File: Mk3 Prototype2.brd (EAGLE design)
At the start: 119.6 x 68 mm, 154 parts, among them IC1 TPD3E001DRL, IC2 TPS62082, IC3 STM32F401V, IC4 BQ24092, IC6 CC3100MOD, IC7 BQ2970, IC8 LSM6DS3, IC9 LIS3MDL, J1 ZX62-AB-5PA(11), J2 ER-TFT024-3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

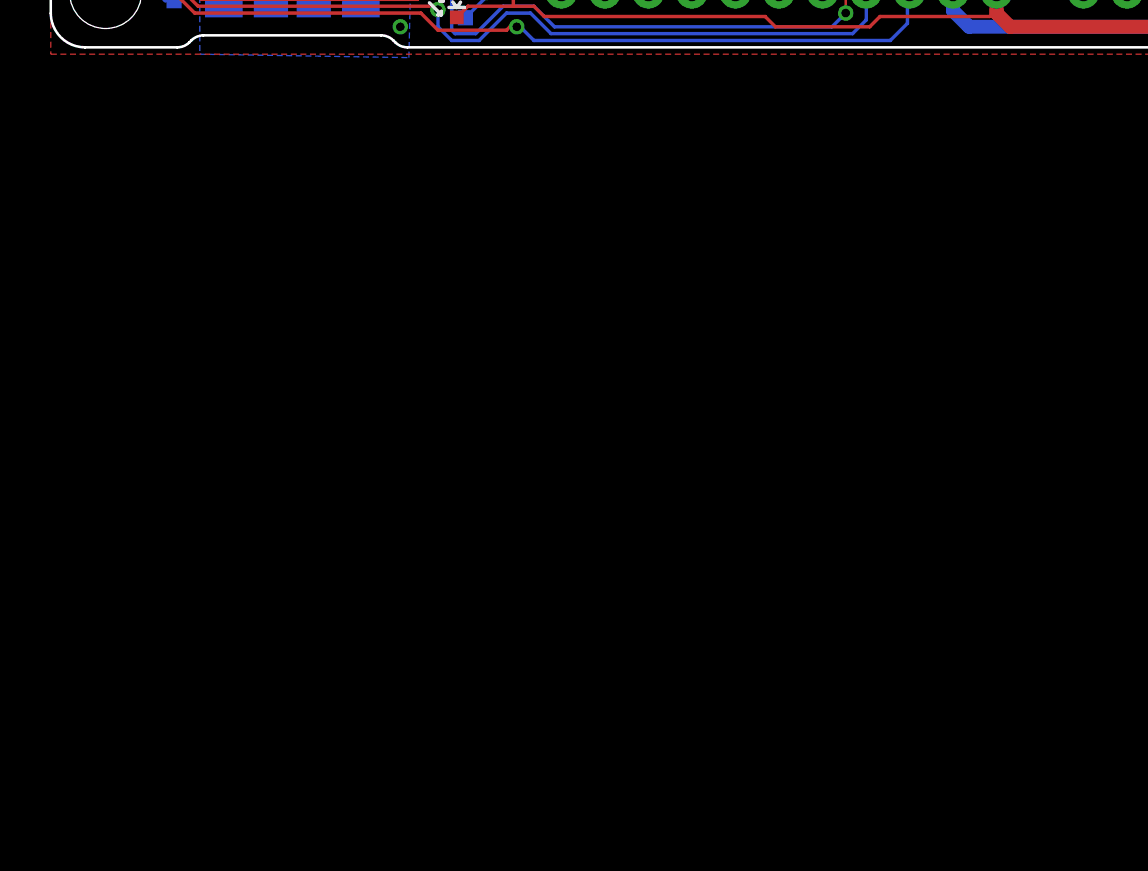
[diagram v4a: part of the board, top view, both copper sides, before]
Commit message: Add full part for LCD out line. update LCD connector to connector part update some resistor parts name
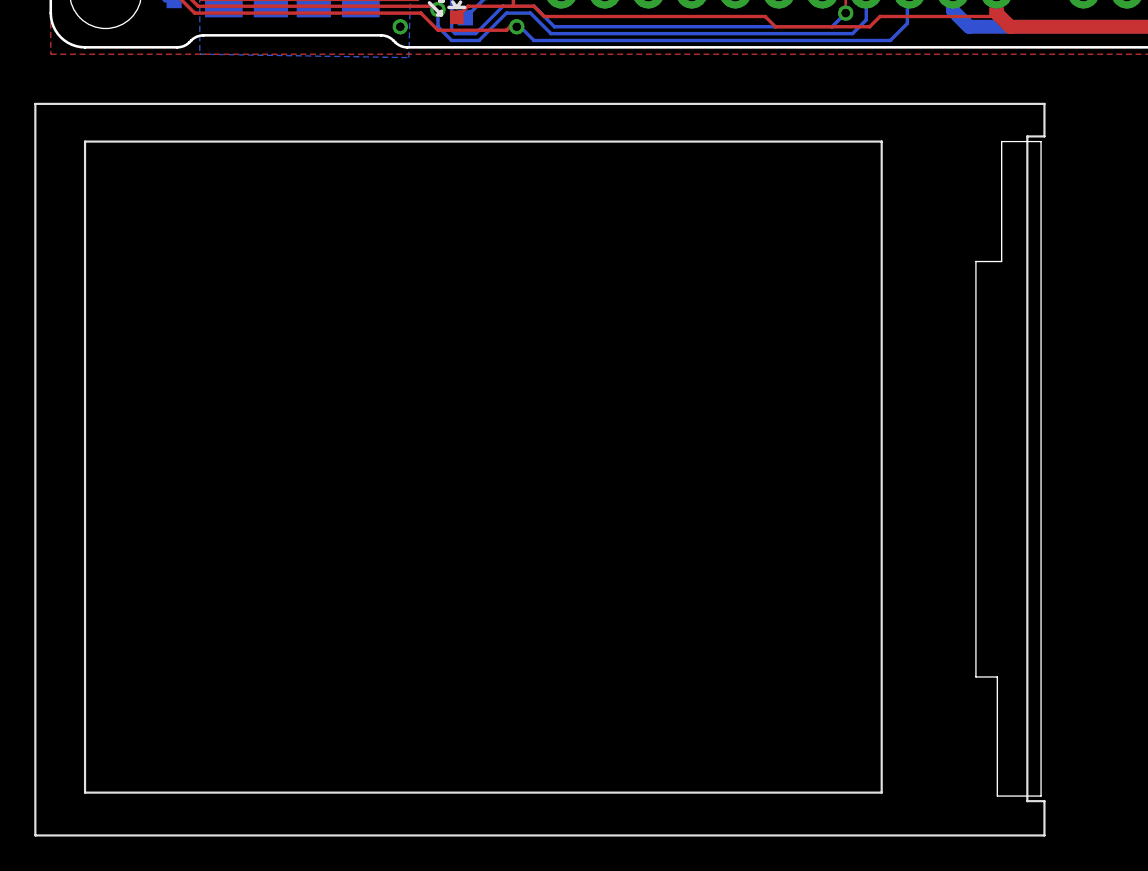
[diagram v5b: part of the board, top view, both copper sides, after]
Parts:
- added U2: ER-TFT024-3, TiLDA Mk3 Parts:ER-TFT024-3
- J2: value ER-TFT024-3 -> ER-CON50HT-1
- R28, R29: value 0603/4.7M/5% -> 0603/4M7/5%
- R44, R47, R48, R49: value 0603/4.7/5% -> 0603/4R7/5%
- U$2: value (none) -> ER-TFT024-3
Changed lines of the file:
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@@
 <variant name="L4" populate="no"/>
 </element>
-<element name="R47" library="TiLDA Mk3 Parts" package="C0603K-SMALL" value="0603/4.7/5%" x="69.6" y="59.2" smashed="yes" rot="MR270">
+<element name="R47" library="TiLDA Mk3 Parts" package="C0603K-SMALL" value="0603/4R7/5%" x="69.6" y="59.2" smashed="yes" rot="MR270">
 <attribute name="NAME" x="69.05" y="54.8" size="1.016" layer="26" font="vector" ratio="14" rot="MR90"/>
 <attribute name="FARNELL" value="9331280" x="69.6" y="59.2" size="1.778" layer="28" rot="MR270" display="off"/>
 <attribute name="FARNELL_REEL" value="2130678" x="69.6" y="59.2" size="1.778" layer="28" rot="MR270" display="off"/>
 </element>
-<element name="R48" library="TiLDA Mk3 Parts" package="C0603K-SMALL" value="0603/4.7/5%" x="71.2" y="59.2" smashed="yes" rot="MR270">
+<element name="R48" library="TiLDA Mk3 Parts" package="C0603K-SMALL" value="0603/4R7/5%" x="71.2" y="59.2" smashed="yes" rot="MR270">
 <attribute name="NAME" x="70.65" y="54.8" size="1.016" layer="26" font="vector" ratio="14" rot="MR90"/>
 <attribute name="FARNELL" value="9331280" x="71.2" y="59.2" size="1.778" layer="28" rot="MR270" display="off"/>
 <attribute name="FARNELL_REEL" value="2130678" x="71.2" y="59.2" size="1.778" layer="28" rot="MR270" display="off"/>
 </element>
-<element name="R49" library="TiLDA Mk3 Parts" package="C0603K-SMALL" value="0603/4.7/5%" x="72.8" y="59.2" smashed="yes" rot="MR270">
+<element name="R49" library="TiLDA Mk3 Parts" package="C0603K-SMALL" value="0603/4R7/5%" x="72.8" y="59.2" smashed="yes" rot="MR270">
 <attribute name="NAME" x="72.25" y="54.8" size="1.016" layer="26" font="vector" ratio="14" rot="MR90"/>
 <attribute name="FARNELL" value="9331280" x="72.8" y="59.2" size="1.778" layer="28" rot="MR270" display="off"/>
@@
 <attribute name="NAME" x="58" y="31.8" size="1.016" layer="26" font="vector" ratio="14" rot="MR0"/>
 </element>
-<element name="J2" library="TiLDA Mk3 Parts" package="FH12-50S-0.5SH" value="ER-TFT024-3" x="65.6" y="41.2" smashed="yes" rot="MR270">
+<element name="J2" library="TiLDA Mk3 Parts" package="FH12-50S-0.5SH" value="ER-CON50HT-1" x="65.6" y="41.2" smashed="yes" rot="MR270">
 <attribute name="NAME" x="61.505" y="55.1476" size="1.016" layer="26" font="vector" ratio="14" rot="MR270"/>
 </element>
-<element name="U$2" library="TiLDA Mk3 Parts" package="ER-TFT024-3" value="" x="35.2" y="19.6" smashed="yes"/>
-<element name="R44" library="TiLDA Mk3 Parts" package="C0603K-SMALL" value="0603/4.7/5%" x="74.4" y="59.2" smashed="yes" rot="MR270">
+<element name="U$2" library="TiLDA Mk3 Parts" package="ER-TFT024-3" value="ER-TFT024-3" x="35.2" y="19.6" smashed="yes"/>
+<element name="R44" library="TiLDA Mk3 Parts" package="C0603K-SMALL" value="0603/4R7/5%" x="74.4" y="59.2" smashed="yes" rot="MR270">
 <attribute name="NAME" x="73.85" y="54.8" size="1.016" layer="26" font="vector" ratio="14" rot="MR90"/>
 <attribute name="FARNELL" value="9331280" x="74.4" y="59.2" size="1.778" layer="28" rot="MR270" display="off"/>
@@
 <variant name="L4" value="0603/10k/5%"/>
 </element>
-<element name="R28" library="TiLDA Mk3 Parts" package="C0603K-SMALL" value="0603/4.7M/5%" x="55.6" y="52" smashed="yes" rot="MR180">
+<element name="R28" library="TiLDA Mk3 Parts" package="C0603K-SMALL" value="0603/4M7/5%" x="55.6" y="52" smashed="yes" rot="MR180">
 <attribute name="NAME" x="54" y="51.35" size="1.016" layer="26" font="vector" ratio="14" rot="MR180"/>
 <attribute name="VALUE" x="54.8" y="53.65" size="1.016" layer="28" rot="MR180"/>
 <attribute name="FARNELL" value="2059694" x="55.6" y="52" size="1.778" layer="28" rot="MR180" display="off"/>
 </element>
-<element name="R29" library="TiLDA Mk3 Parts" package="C0603K-SMALL" value="0603/4.7M/5%" x="52" y="55.6" smashed="yes" rot="MR90">
+<element name="R29" library="TiLDA Mk3 Parts" package="C0603K-SMALL" value="0603/4M7/5%" x="52" y="55.6" smashed="yes" rot="MR90">
 <attribute name="NAME" x="51.45" y="57.2" size="1.016" layer="26" font="vector" ratio="14" rot="MR90"/>
 <attribute name="VALUE" x="50.35" y="54.8" size="1.016" layer="28" rot="MR90"/>
@@
 <variant name="L4" populate="no"/>
 </element>
+<element name="U2" library="TiLDA Mk3 Parts" package="ER-TFT024-3" value="ER-TFT024-3" x="4" y="-46"/>
 </elements>
 <signals>

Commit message: Give power switch a value
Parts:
- S5: value (none) -> Power Switch
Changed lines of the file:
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@@
 <attribute name="NAME" x="5.3985" y="2.911" size="1.016" layer="26" font="vector" ratio="14" rot="MR90"/>
 </element>
-<element name="S5" library="TiLDA Mk3 Parts" package="SWITCH-SPST-SMD-A" value="" x="60.3" y="60.9" smashed="yes" rot="MR0">
+<element name="S5" library="TiLDA Mk3 Parts" package="SWITCH-SPST-SMD-A" value="Power Switch" x="60.3" y="60.9" smashed="yes" rot="MR0">
 <attribute name="NAME" x="61.17" y="60.935" size="1.016" layer="26" font="vector" ratio="14" rot="MR0"/>
 <attribute name="VALUE" x="61.57" y="59.63" size="0.6096" layer="28" rot="MR0"/>

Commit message: updating usb resitors
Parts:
- R23, R25: value 0603/22/1% -> 0603/0R
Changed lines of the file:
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@@
 <attribute name="NAME" x="21.875" y="44.6475" size="1.016" layer="26" font="vector" ratio="14" rot="MR180"/>
 </element>
-<element name="R23" library="TiLDA Mk3 Parts" package="C0603K-SMALL" value="0603/22/1%" x="16.4" y="19.6" smashed="yes" rot="MR0">
+<element name="R23" library="TiLDA Mk3 Parts" package="C0603K-SMALL" value="0603/0R" x="16.4" y="19.6" smashed="yes" rot="MR0">
 <attribute name="NAME" x="18" y="20" size="1.016" layer="26" font="vector" ratio="14" rot="MR180"/>
 </element>
-<element name="R25" library="TiLDA Mk3 Parts" package="C0603K-SMALL" value="0603/22/1%" x="16.4" y="20.8" smashed="yes" rot="MR0">
+<element name="R25" library="TiLDA Mk3 Parts" package="C0603K-SMALL" value="0603/0R" x="16.4" y="20.8" smashed="yes" rot="MR0">
 <attribute name="NAME" x="18" y="21.2" size="1.016" layer="26" font="vector" ratio="14" rot="MR180"/>
 </element>
